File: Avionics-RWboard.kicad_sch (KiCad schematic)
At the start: 4 parts

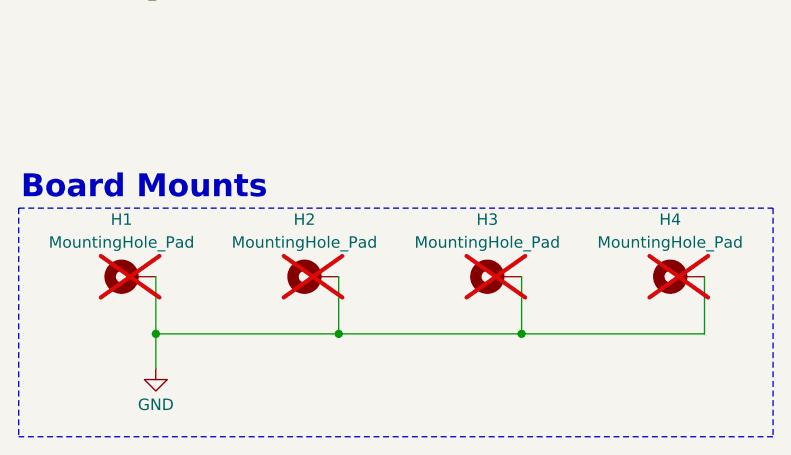
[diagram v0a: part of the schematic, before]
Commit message: moved inductor and added leds
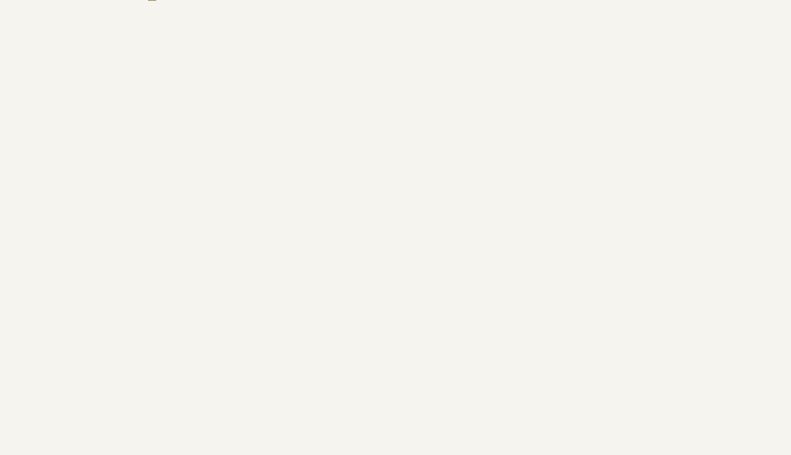
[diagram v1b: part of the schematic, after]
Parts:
- removed H1, H2, H3, H4: MountingHole_Pad, MountingHole:MountingHole_3.2mm_M3_Pad_Via, symbol Mechanical:MountingHole_Pad
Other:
- note removed: "Board Mounts"
